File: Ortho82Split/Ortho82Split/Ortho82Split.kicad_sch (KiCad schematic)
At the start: 109 parts, among them J3 USB_C_Receptacle_USB2.0, J6 Conn_01x06_Socket, J7 Conn_01x08_Socket, J8 Conn_01x06_Socket, J9 TC2030-IDC-NL, SW11 SW_Push, SW12 SW_Push, SW13 SW_Push, SW14 SW_Push, SW15 SW_Push, SW16 SW_Push, SW17 SW_Push, SW18 SW_Push, SW19 SW_Push, SW20 SW_Push, SW21 SW_Push, SW22 SW_Push, SW23 SW_Push, SW24 SW_Push, SW25 SW_Push, SW26 SW_Push, SW27 SW_Push, SW28 SW_Push, SW29 SW_Push, SW30 SW_Push, SW31 SW_Push, SW32 SW_Push, SW33 SW_Push, SW34 SW_Push, SW35 SW_Push, SW36 SW_Push, SW37 SW_Push, SW38 SW_Push, SW39 SW_Push, SW40 SW_Push, SW41 SW_Push, SW42 SW_Push, SW43 SW_Push, SW44 SW_Push, SW45 SW_Push, SW46 SW_Push, SW47 SW_Push, SW48 SW_Push, SW49 SW_Push, SW50 SW_Push, SW51 SW_Push, SW74 OS, SW83 SW_Push, U1 MCP1700T-3302E_TT, U2 ATxmega32A4U-A, U3 USBLC6-2SC6

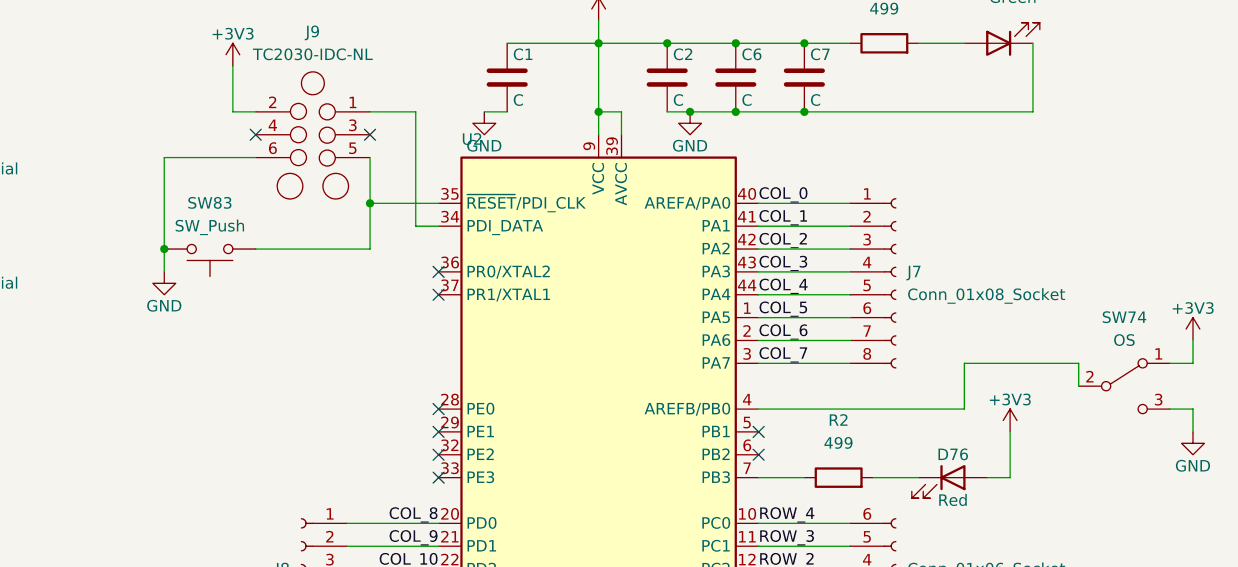
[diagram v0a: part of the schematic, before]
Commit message: Corrects spacing between keyswitches.
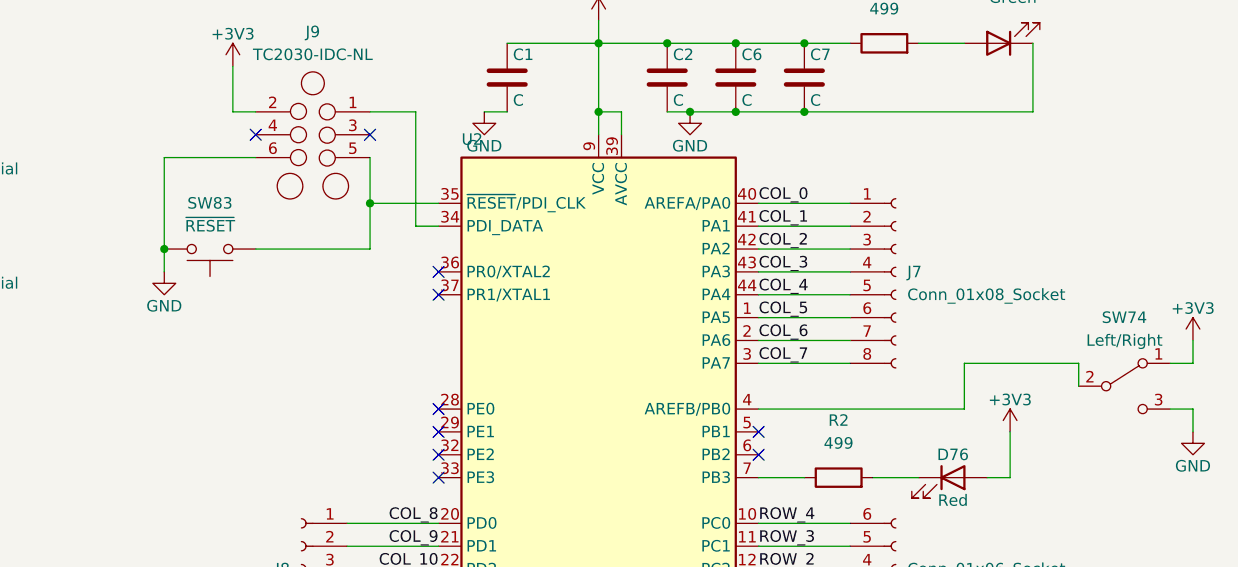
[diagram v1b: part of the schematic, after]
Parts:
- D11, D12, D13, D14, D15, D16, D17, D18, D19, D20, D21, D22, D23, D24, D25, D26, D27, D28, D29, D30, D31, D32, D33, D34, D35, D36, D37, D38, D39, D40, D41, D42, D43, D44, D45, D46, D47, D48, D49, D50, D51: footprint Diode_SMD:D_SOD-123 -> HandsolderModifiedComponents:D_SOD-123F_DoubleSided
- SW74: value OS -> Left/Right; footprint Button_Switch_SMD:SW_SPDT_CK-JS102011SAQN -> Jumper:SolderJumper-3_P2.0mm_Open_TrianglePad1.0x1.5mm_NumberLabels
- SW83: value SW_Push -> ~{RESET}; footprint Button_Switch_SMD:SW_Tactile_SPST_NO_Straight_CK_PTS636Sx25SMTRLFS -> Jumper:SolderJumper-2_P1.3mm_Open_RoundedPad1.0x1.5mm

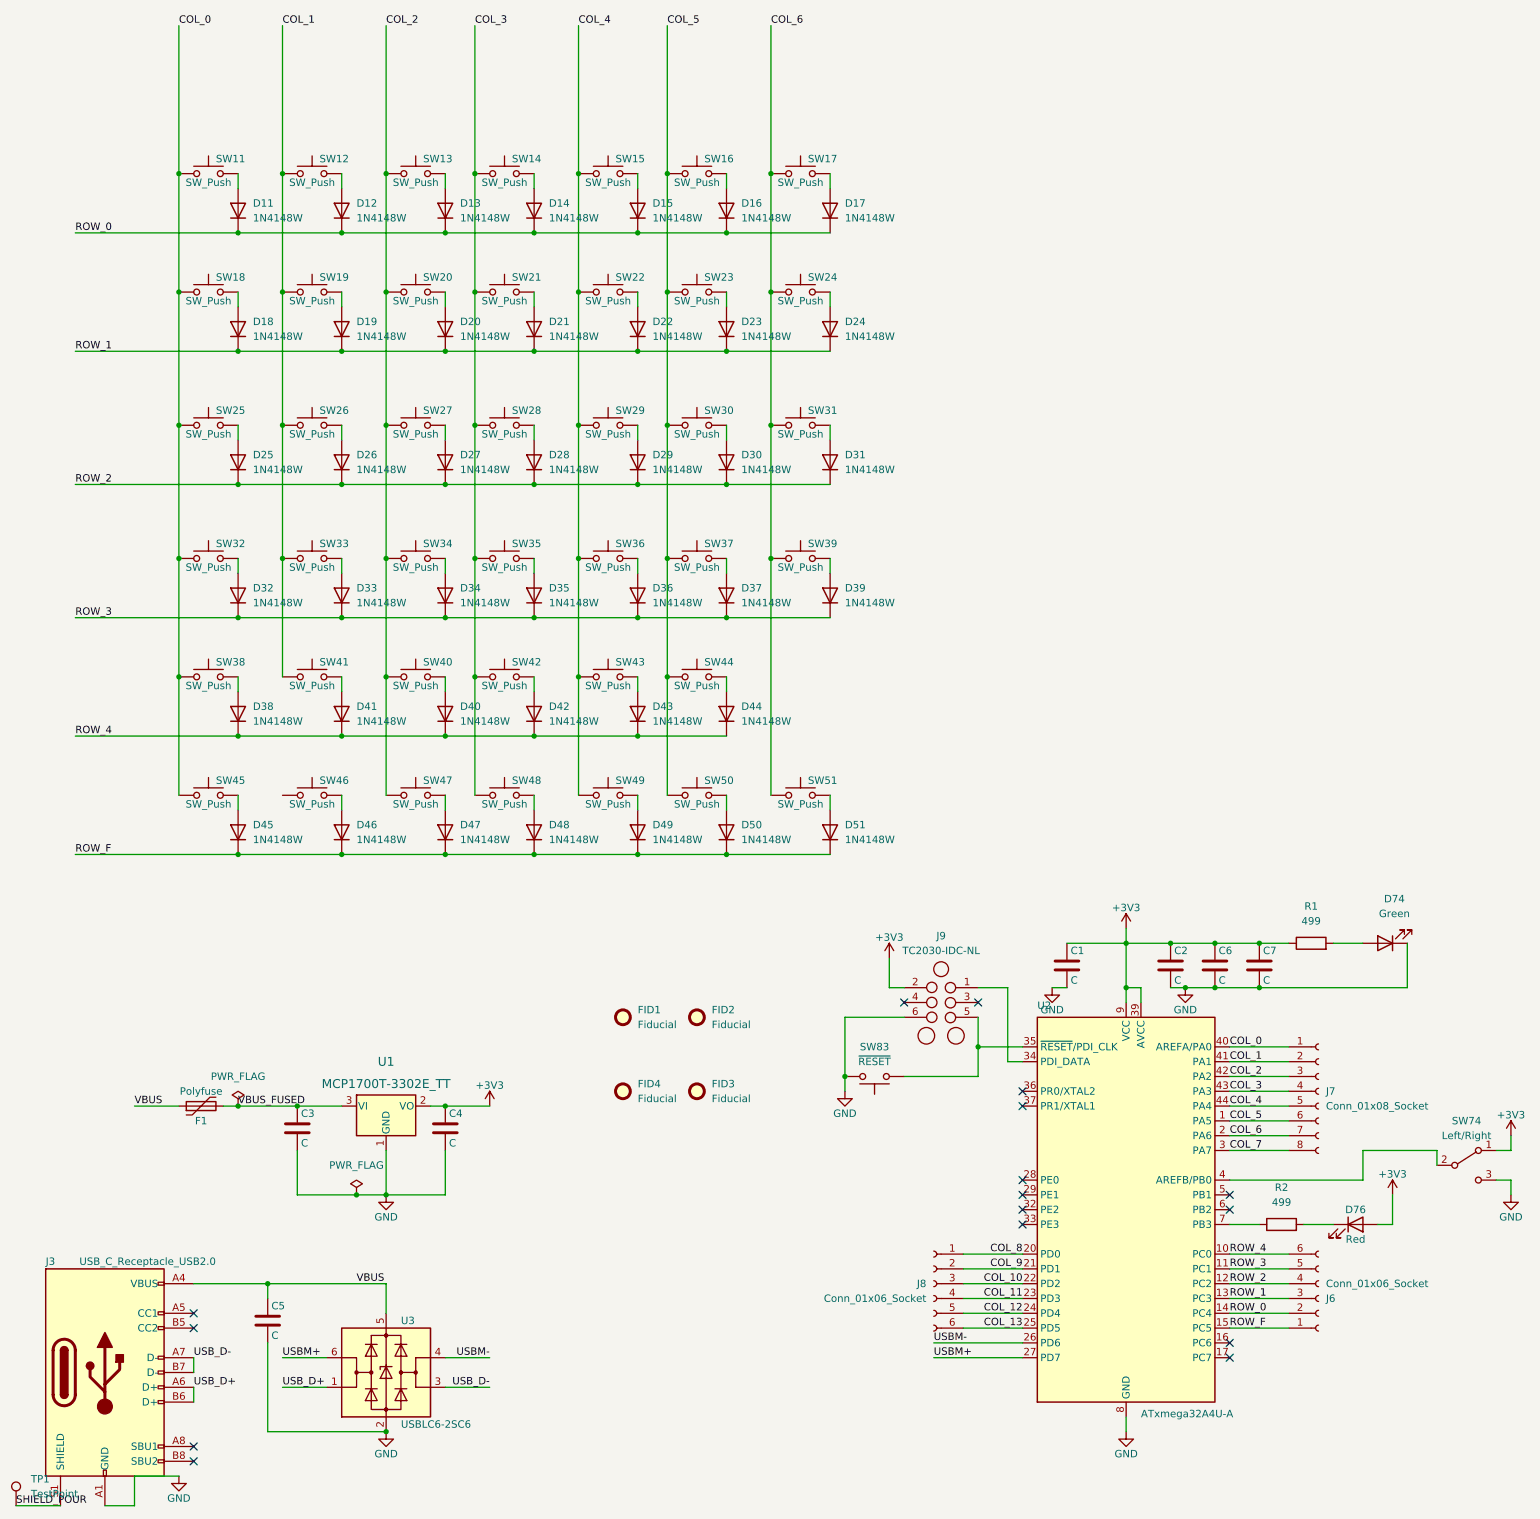
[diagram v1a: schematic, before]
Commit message: Route USB and xmega circuit.
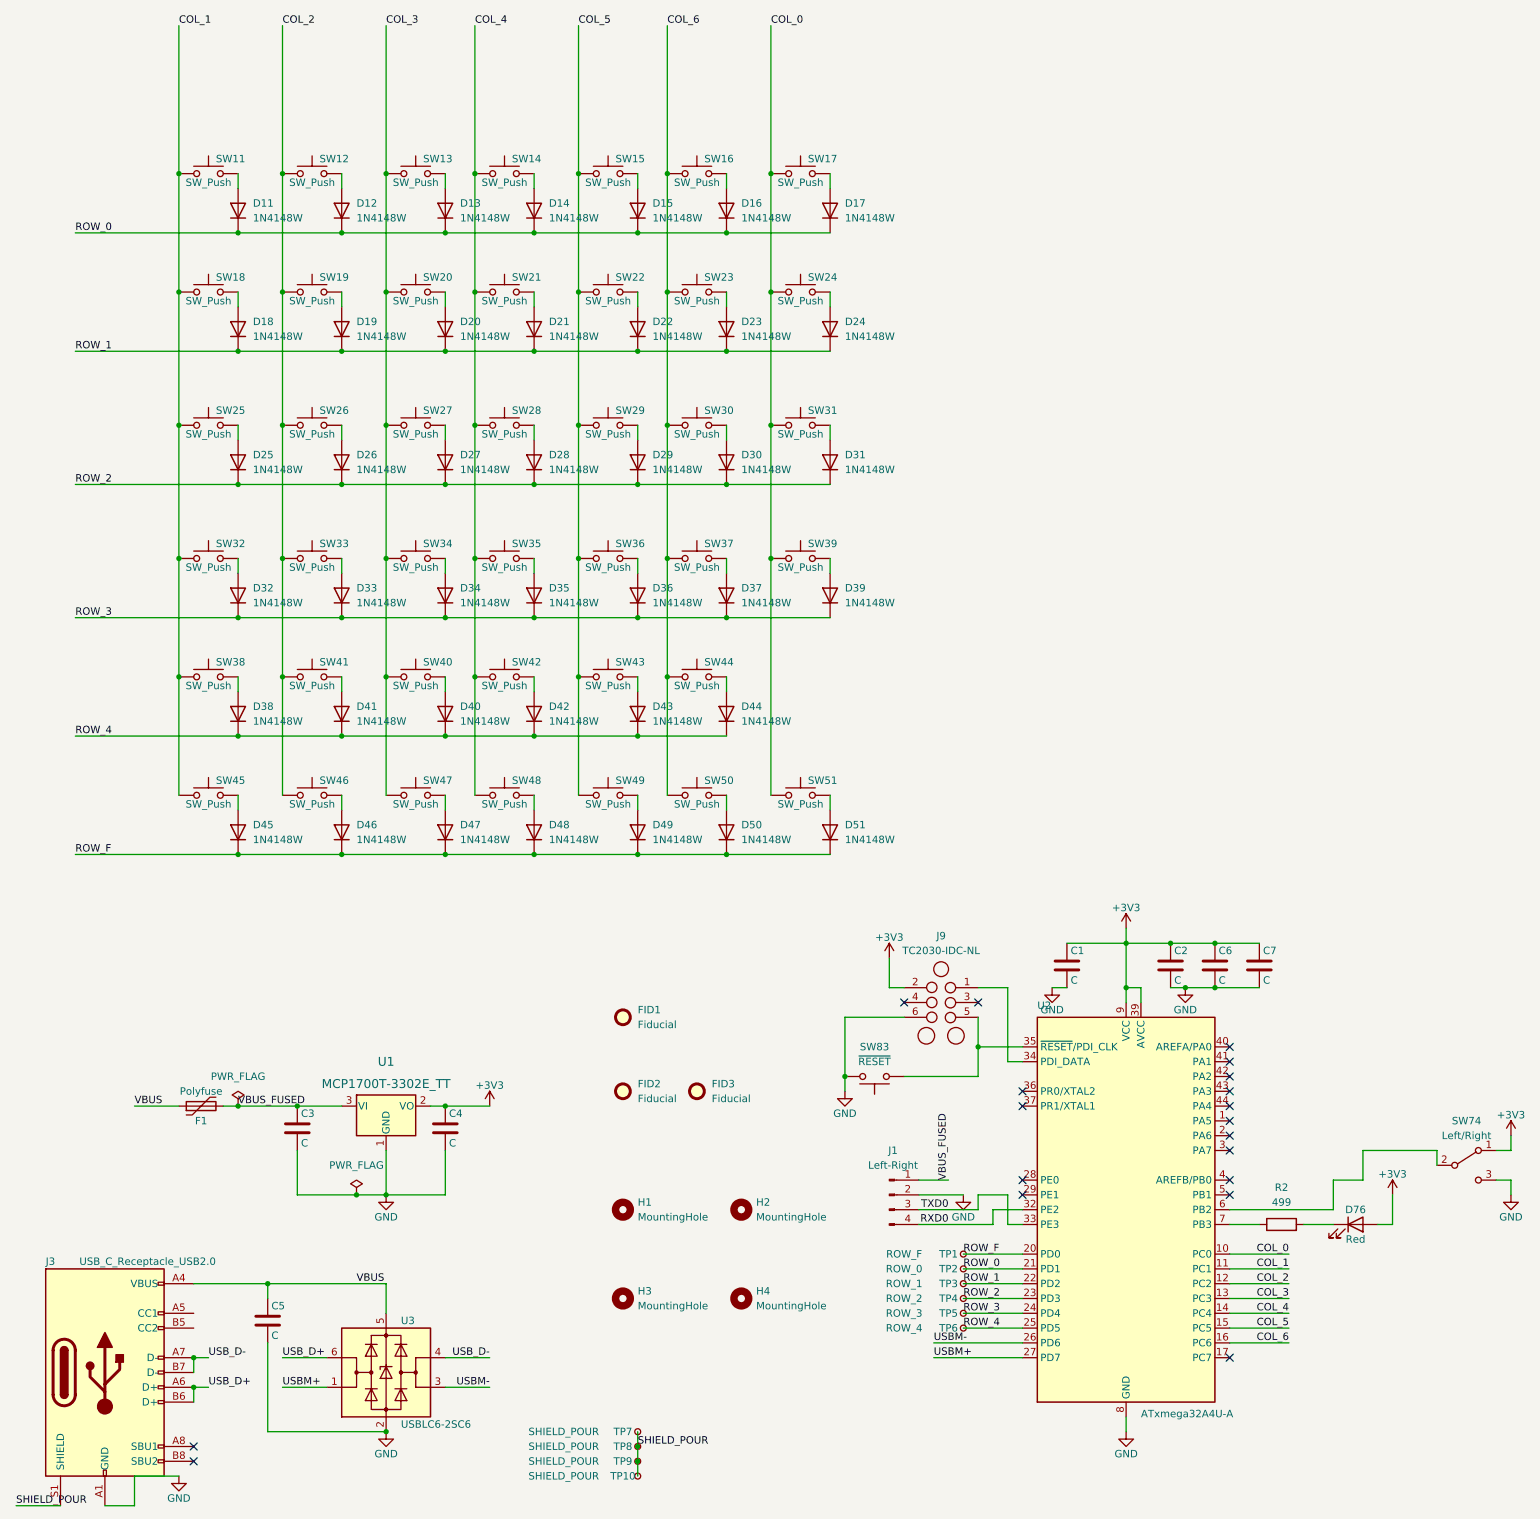
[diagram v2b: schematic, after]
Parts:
- removed D74: Green, LED_SMD:LED_0805_2012Metric_Pad1.15x1.40mm_HandSolder, symbol Device:LED
- removed FID2: Fiducial, Fiducial:Fiducial_0.5mm_Mask1mm, symbol Mechanical:Fiducial
- removed J6, J8: Conn_01x06_Socket, Connector_PinHeader_1.27mm:PinHeader_1x06_P1.27mm_Vertical, symbol Connector:Conn_01x06_Socket
- removed J7: Conn_01x08_Socket, Connector_PinHeader_1.27mm:PinHeader_1x08_P1.27mm_Vertical, symbol Connector:Conn_01x08_Socket
- removed R1: 499, Resistor_SMD:R_0805_2012Metric_Pad1.20x1.40mm_HandSolder, symbol Device:R
- removed TP1: TestPoint, TestPoint:TestPoint_Pad_D1.0mm, symbol Connector:TestPoint
- added H1, H2, H3, H4: MountingHole, MountingHole:MountingHole_3.2mm_M3, symbol Mechanical:MountingHole
- added J1: Left-Right, Connector_PinHeader_2.00mm:PinHeader_1x04_P2.00mm_Vertical, symbol Connector:Conn_01x04_Pin
- added TP1: ROW_F, TestPoint:TestPoint_THTPad_1.5x1.5mm_Drill0.7mm, symbol Connector:TestPoint_Small
- added TP10, TP7, TP8, TP9: SHIELD_POUR, TestPoint:TestPoint_THTPad_1.5x1.5mm_Drill0.7mm, symbol Connector:TestPoint_Small
- added TP2: ROW_0, TestPoint:TestPoint_THTPad_1.5x1.5mm_Drill0.7mm, symbol Connector:TestPoint_Small
- added TP3: ROW_1, TestPoint:TestPoint_THTPad_1.5x1.5mm_Drill0.7mm, symbol Connector:TestPoint_Small
- added TP4: ROW_2, TestPoint:TestPoint_THTPad_1.5x1.5mm_Drill0.7mm, symbol Connector:TestPoint_Small
- added TP5: ROW_3, TestPoint:TestPoint_THTPad_1.5x1.5mm_Drill0.7mm, symbol Connector:TestPoint_Small
- added TP6: ROW_4, TestPoint:TestPoint_THTPad_1.5x1.5mm_Drill0.7mm, symbol Connector:TestPoint_Small
- D76: footprint LED_SMD:LED_0805_2012Metric_Pad1.15x1.40mm_HandSolder -> LED_THT:LED_D3.0mm
- R2: footprint LED_SMD:LED_0805_2012Metric_Pad1.15x1.40mm_HandSolder -> Resistor_SMD:R_0805_2012Metric_Pad1.20x1.40mm_HandSolder
- SW74: footprint Jumper:SolderJumper-3_P2.0mm_Open_TrianglePad1.0x1.5mm_NumberLabels -> Jumper:SolderJumper-3_P1.3mm_Open_RoundedPad1.0x1.5mm_NumberLabels
- SW83: footprint Jumper:SolderJumper-2_P1.3mm_Open_RoundedPad1.0x1.5mm -> Button_Switch_SMD:SW_Tactile_SPST_NO_Straight_CK_PTS636Sx25SMTRLFS
- renumbered FID4 to FID2
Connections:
- net COL_10 is gone; now on net ROW_1: U2.22 (PD2)
- net COL_11 is gone; now on net ROW_2: U2.23 (PD3)
- net COL_12 is gone; now on net ROW_3: U2.24 (PD4)
- net COL_13 is gone; now on net ROW_4: U2.25 (PD5)
- net COL_8 is gone; now on net ROW_F: U2.20 (PD0)
- net COL_9 is gone; now on net ROW_0: U2.21 (PD1)
- net COL_0: now also SW17.1, SW24.1, SW31.1, SW39.1, SW51.1, U2.10 (PC0); no longer SW11.1, SW18.1, SW25.1, SW32.1, SW38.1, SW45.1, U2.40 (AREFA/PA0)
- net COL_1: now also SW11.1, SW18.1, SW25.1, SW32.1, SW38.1, SW45.1, U2.11 (PC1); no longer SW12.1, SW19.1, SW26.1, SW33.1, SW41.1, U2.41 (PA1)
- net COL_2: now also SW12.1, SW19.1, SW26.1, SW33.1, SW41.1, SW46.1, U2.12 (PC2); no longer SW13.1, SW20.1, SW27.1, SW34.1, SW40.1, SW47.1, U2.42 (PA2)
- net COL_3: now also SW13.1, SW20.1, SW27.1, SW34.1, SW40.1, SW47.1, U2.13 (PC3); no longer SW14.1, SW21.1, SW28.1, SW35.1, SW42.1, SW48.1, U2.43 (PA3)
- net COL_4: now also SW14.1, SW21.1, SW28.1, SW35.1, SW42.1, SW48.1, U2.14 (PC4); no longer SW15.1, SW22.1, SW29.1, SW36.1, SW43.1, SW49.1, U2.44 (PA4)
- net COL_5: now also SW15.1, SW22.1, SW29.1, SW36.1, SW43.1, SW49.1, U2.15 (PC5); no longer SW16.1, SW23.1, SW30.1, SW37.1, SW44.1, SW50.1, U2.1 (PA5)
- net COL_6: now also SW16.1, SW23.1, SW30.1, SW37.1, SW44.1, SW50.1, U2.16 (PC6); no longer SW17.1, SW24.1, SW31.1, SW39.1, SW51.1, U2.2 (PA6)
- net GND: now also J1.2 (Pin_2)
- net ROW_0: now also TP2.1; no longer U2.14 (PC4)
- net ROW_1: now also TP3.1; no longer U2.13 (PC3)
- net ROW_2: now also TP4.1; no longer U2.12 (PC2)
- net ROW_3: now also TP5.1; no longer U2.11 (PC1)
- net ROW_4: now also TP6.1; no longer U2.10 (PC0)
- net ROW_F: now also TP1.1; no longer U2.15 (PC5)
- net SHIELD_POUR: now also TP10.1, TP7.1, TP8.1, TP9.1
- net USBM+: now also U3.1 (I/O1); no longer U3.6 (I/O1)
- net USBM-: now also U3.3 (I/O2); no longer U3.4 (I/O2)
- net USB_D+: now also U3.6 (I/O1); no longer U3.1 (I/O1)
- net USB_D-: now also U3.4 (I/O2); no longer U3.3 (I/O2)
- net VBUS_FUSED: now also J1.1 (Pin_1)
- net RXD0: now reaches U2.32 (PE2)
- net RXD0: now also J1.4 (Pin_4)
- net TXD0: now reaches U2.33 (PE3)
- net TXD0: now also J1.3 (Pin_3)
- net at U2.4 (AREFB/PB0): no longer SW74.2 (B)
- net at U2.6 (PB2): now also SW74.2 (B)
- net COL_7: no longer names the net of U2.3 (PA7)
- no-connect marks 16 -> 19

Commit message: Adds USB current resistors.
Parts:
- added R1, R3: 5.1k, Resistor_SMD:R_0805_2012Metric_Pad1.20x1.40mm_HandSolder, symbol Device:R
- C1, C2, C6, C7: value C -> 100n
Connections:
- net GND: now also R1.2, R3.2
- net at J3.A5 (CC1): now also R1.1
- net at J3.B5 (CC2): now also R3.1
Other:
- moved on the sheet: C1, C2, C3, C4, C5, C6, C7, D76, F1, FID1, FID2, FID3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

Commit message: Document and tidyup schematic.
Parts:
- C3, C4, C5: value C -> 1u
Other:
- note added: "ASDFG Row"
- note added: "Function Row"
- note added: "MetaSpc Row"
- note added: "Numbers Row"
- note added: "QWERTY Row"
- note added: "ZXCVB Row"
- title: 66 Keys Ortholinear Keyboard -> 82 Keys Ortholinear Keyboard
- moved on the sheet: C1, C2, C3, C4, C5, C6, C7, D11, D12, D13, D14, D15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

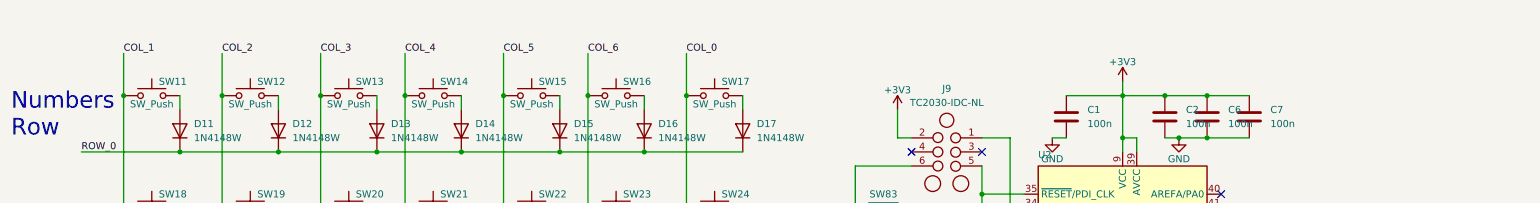
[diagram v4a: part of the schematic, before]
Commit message: Update documentation on schematic and PCB.
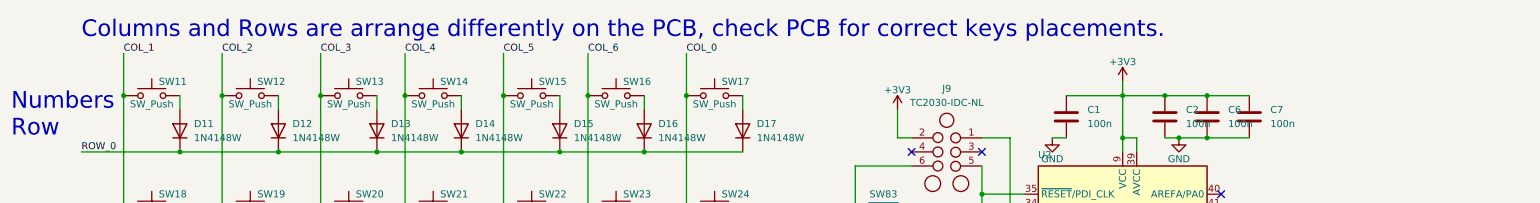
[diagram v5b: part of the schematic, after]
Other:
- note added: "Columns and Rows are arrange differently on the PCB, check PCB for correct keys placements."
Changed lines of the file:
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@@
   (title_block
     (title "82 Keys Ortholinear Keyboard")
-    (rev "1.0")
+    (rev "1.0-doc1")
     (company "125 Systems")
     (comment 1 "Designer: Neeraj Adsul")
@@
     (effects (font (face "Arial") (size 3 3) (color 72 0 72 1)) (justify left bottom))
   )
+  (text "Columns and Rows are arrange differently on the PCB, check PCB for correct keys placements."
+    (at 25.4 20.32 0)
+    (effects (font (face "Arial") (size 3 3) (color 72 0 72 1)) (justify left bottom))
+  )
